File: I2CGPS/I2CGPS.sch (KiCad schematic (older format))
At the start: 1 part, among them P1 CONN_01X05

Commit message: I2C-GPS initial design
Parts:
- added C1, C2: C, Capacitors_SMD:C_1210_HandSoldering, symbol C
- added P2, P3: CONN_01X09, Pin_Headers:Pin_Header_Straight_1x09, symbol CONN_01X09
- added U1: GY-NEO6MV2, ADEM:GY-NEO6MV2, symbol GY-NEO6MV2
- added uP1: ARDUPROMINI-6, ArduProMiniTKB:ArduProMini-6, symbol ARDUPROMINI-6
- P1: footprint (none) -> Pin_Headers:Pin_Header_Straight_1x05
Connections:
- net VCC: now reaches P1.1 (P1)
- net VCC: now also C1.1, C2.1, P3.1 (P1), U1.1 (VCC), uP1.22 (Vcc2)
- net SDA: now reaches P1.2 (P2)
- net SDA: now also P2.8 (P8), uP1.11 (D2)
- net SCL: now reaches P1.3 (P3)
- net SCL: now also P2.7 (P7), uP1.12 (D3)
- net INT: now reaches P1.4 (P4)
- net INT: now also P2.6 (P6), uP1.13 (D4)
- net GND: now reaches P1.5 (P5)
- net GND: now also C1.2, C2.2, P2.9 (P9), U1.4 (GND), uP1.10 (GND), uP1.20 (GND3)
- new net: P2.5 (P5), uP1.14 (D5)
- new net: P2.4 (P4), uP1.15 (D6)
- new net: P2.3 (P3), uP1.16 (D7)
- new net: P2.2 (P2), uP1.17 (D8)
- new net: P2.1 (P1), uP1.18 (D9)
- new net: P3.2 (P2), uP1.23 (A3)
- new net: P3.3 (P3), uP1.24 (A2)
- new net: P3.4 (P4), uP1.25 (A1)
- new net: P3.5 (P5), uP1.26 (A0)
- new net: P3.6 (P6), uP1.27 (D13)
- new net: P3.7 (P7), uP1.28 (D12)
- new net: P3.8 (P8), uP1.29 (D11)
- new net: P3.9 (P9), uP1.30 (D10)
- new net RX: U1.2 (RX), uP1.8 (RX1)
- new net TX: U1.3 (TX), uP1.7 (TX0)

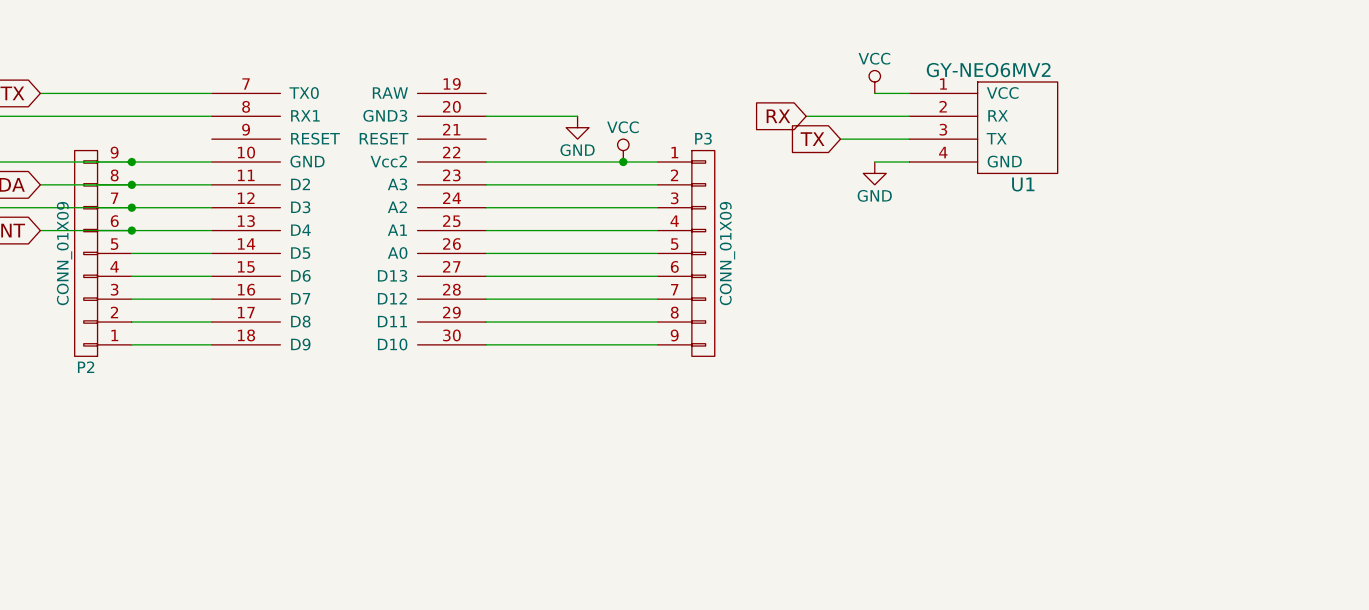
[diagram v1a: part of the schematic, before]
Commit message: IC2 GPS with power down fet
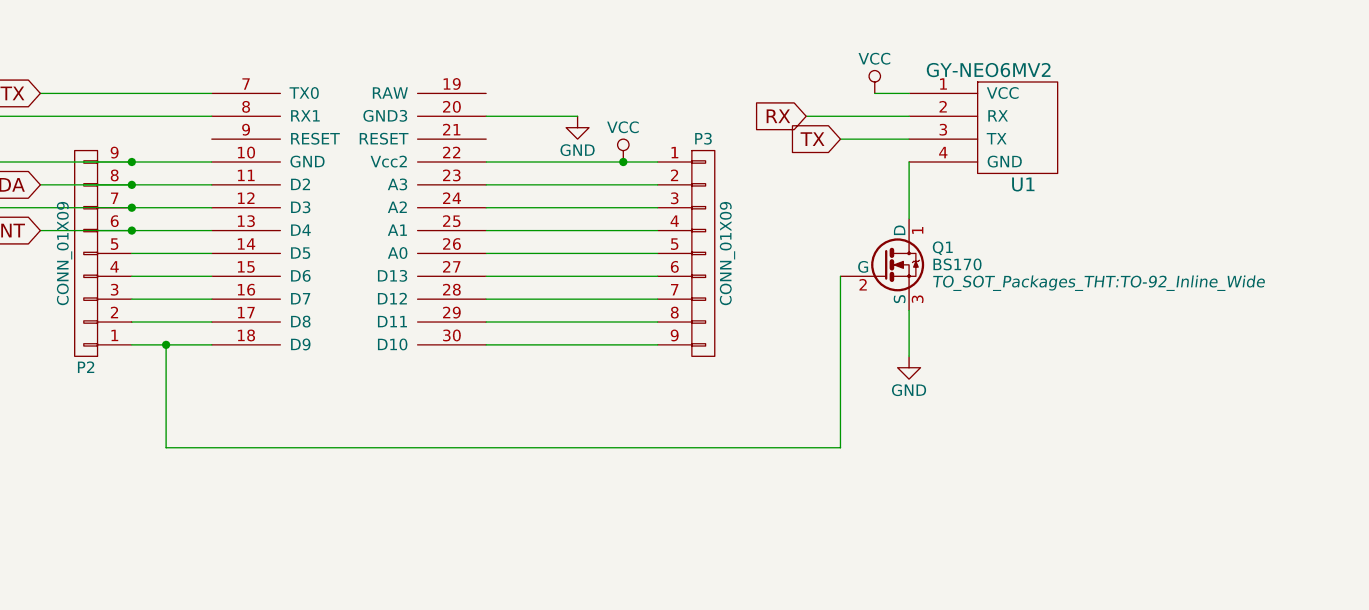
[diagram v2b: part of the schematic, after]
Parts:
- added Q1: BS170, TO_SOT_Packages_THT:TO-92_Inline_Wide, symbol BS170
- P1: footprint Pin_Headers:Pin_Header_Straight_1x05 -> Pin_Headers:Pin_Header_Angled_1x05
- uP1: footprint ArduProMiniTKB:ArduProMini-6 -> ArduProMiniTKB:ArduProMini
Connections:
- net GND: now also Q1.3 (S); no longer U1.4 (GND)
- net at P2.1 (P1), uP1.18 (D9): now also Q1.2 (G)
- new net: Q1.1 (D), U1.4 (GND)
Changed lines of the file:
@@
 F 0 "P1" H 1800 1900 50  0000 C CNN
 F 1 "CONN_01X05" V 1900 1600 50  0000 C CNN
-F 2 "Pin_Headers:Pin_Header_Straight_1x05" H 1800 1600 50  0001 C CNN
+F 2 "Pin_Headers:Pin_Header_Angled_1x05" H 1800 1600 50  0001 C CNN
 F 3 "" H 1800 1600 50  0000 C CNN
 	1    1800 1600
@@
 F 0 "uP1" H 3200 2500 60  0000 C CNN
 F 1 "ARDUPROMINI-6" H 3400 2600 60  0000 C CNN
-F 2 "ArduProMiniTKB:ArduProMini-6" H 3400 2600 60  0001 C CNN
+F 2 "ArduProMiniTKB:ArduProMini" H 3400 2600 60  0001 C CNN
 F 3 "" H 3400 2600 60  0000 C CNN
 	1    3400 2600
@@
 L GND #PWR03
 U 1 1 57BB5D8A
-P 5100 4000
-F 0 "#PWR03" H 5100 3750 50  0001 C CNN
-F 1 "GND" H 5100 3850 50  0000 C CNN
-F 2 "" H 5100 4000 50  0000 C CNN
-F 3 "" H 5100 4000 50  0000 C CNN
-	1    5100 4000
+P 5250 4850
+F 0 "#PWR03" H 5250 4600 50  0001 C CNN
+F 1 "GND" H 5250 4700 50  0000 C CNN
+F 2 "" H 5250 4850 50  0000 C CNN
+F 3 "" H 5250 4850 50  0000 C CNN
+	1    5250 4850
 	1    0    0    -1
 $EndComp
@@
 Wire Wire Line
 	5100 3700 5250 3700
-Wire Wire Line
-	5100 4000 5250 4000
 Wire Wire Line
 	3400 3800 3800 3800
@@
 	1850 4700 2200 4700
 Wire Wire Line
-	2200 4800 1850 4800
-Wire Wire Line
 	3400 4800 4150 4800
 Wire Wire Line
@@
 	4150 4100 3400 4100
 Connection ~ 4000 4000
+$Comp
+L BS170 Q1
+U 1 1 57BC9FCB
+P 5150 4450
+F 0 "Q1" H 5350 4525 50  0000 L CNN
+F 1 "BS170" H 5350 4450 50  0000 L CNN
+F 2 "TO_SOT_Packages_THT:TO-92_Inline_Wide" H 5350 4375 50  0000 L CIN
+F 3 "" H 5150 4450 50  0000 L CNN
+	1    5150 4450
+	1    0    0    -1
+$EndComp
+Wire Wire Line
+	5250 4000 5250 4250
+Wire Wire Line
+	5250 4650 5250 4850
+Wire Wire Line
+	4950 5250 4950 4500
+Wire Wire Line
+	2000 5250 4950 5250
+Wire Wire Line
+	2200 4800 1850 4800
+Wire Wire Line
+	2000 4800 2000 5250
+Connection ~ 2000 4800
 $EndSCHEMATC

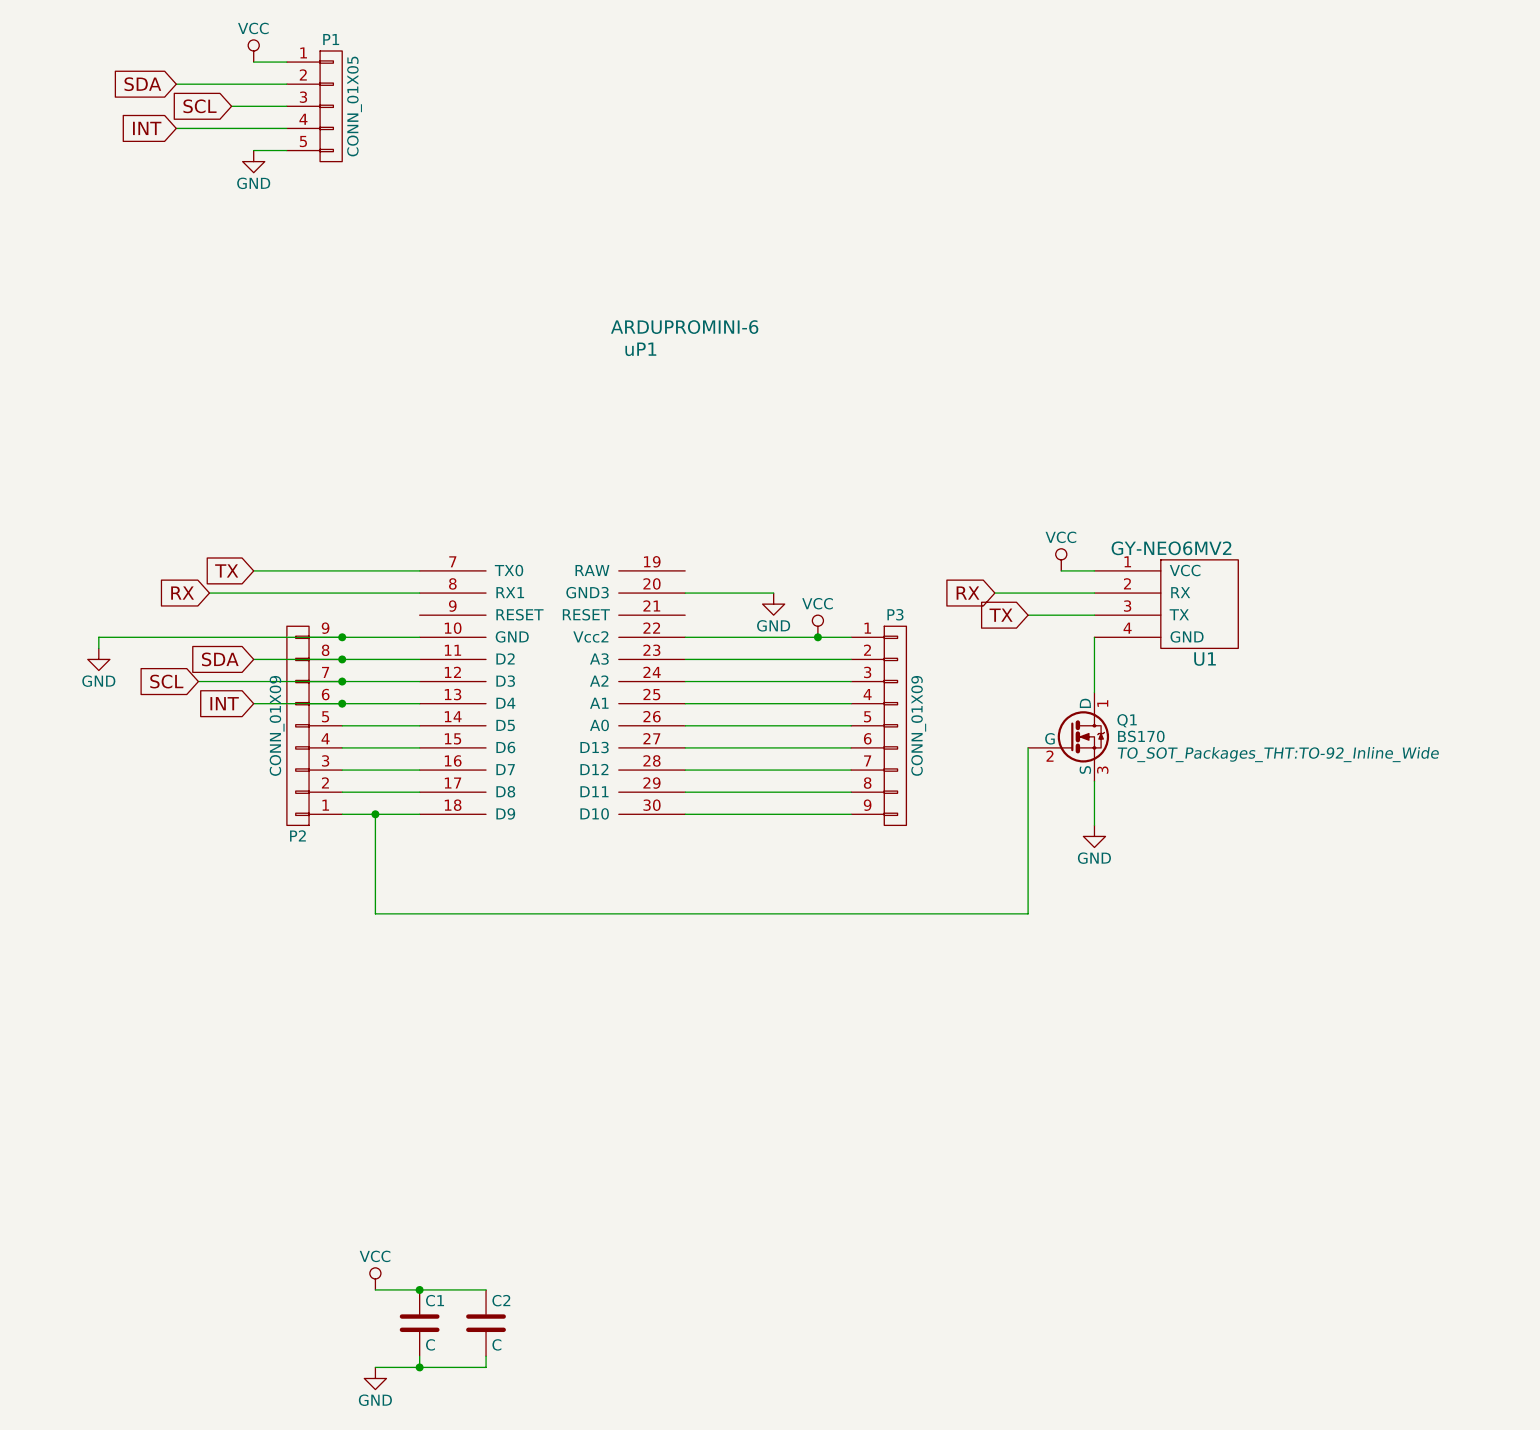
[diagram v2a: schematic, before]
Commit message: resized to particle sensor and panelized
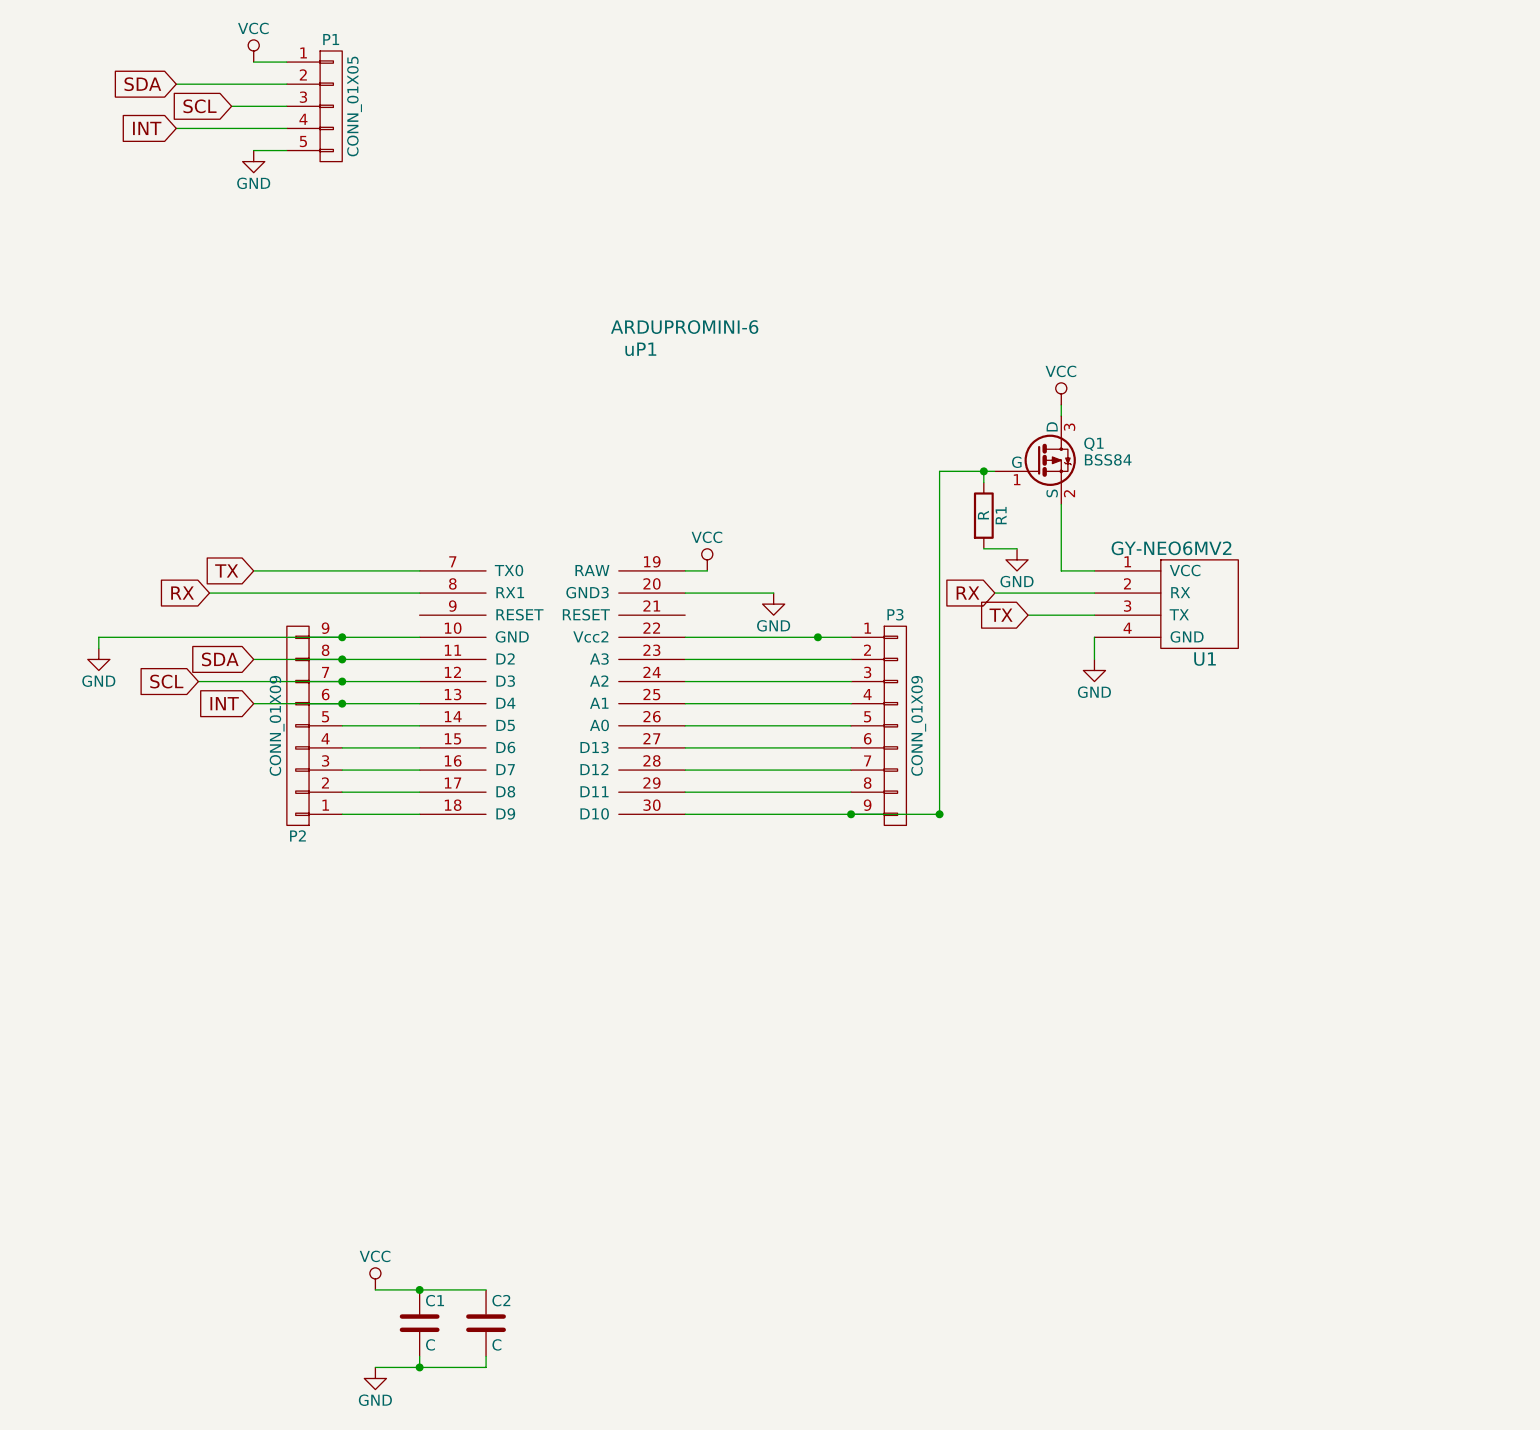
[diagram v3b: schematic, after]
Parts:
- removed Q1: BS170, TO_SOT_Packages_THT:TO-92_Inline_Wide, symbol BS170
- added Q1: BSS84, TO_SOT_Packages_SMD:SOT-23, symbol BSS84
- added R1: R, Resistors_SMD:R_1210_HandSoldering, symbol R
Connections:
- net GND: now also U1.4 (GND), R1.2
- net VCC: now also uP1.19 (RAW), Q1.3 (D); no longer P3.1 (P1), U1.1 (VCC), uP1.22 (Vcc2)
- net at P3.9 (P9), uP1.30 (D10): now also Q1.1 (G), R1.1
- new net: P3.1 (P1), uP1.22 (Vcc2)
- new net: Q1.2 (S), U1.1 (VCC)
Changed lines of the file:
@@
 L GND #PWR03
 U 1 1 57BB5D8A
-P 5250 4850
-F 0 "#PWR03" H 5250 4600 50  0001 C CNN
-F 1 "GND" H 5250 4700 50  0000 C CNN
-F 2 "" H 5250 4850 50  0000 C CNN
-F 3 "" H 5250 4850 50  0000 C CNN
-	1    5250 4850
+P 5250 4100
+F 0 "#PWR03" H 5250 3850 50  0001 C CNN
+F 1 "GND" H 5250 3950 50  0000 C CNN
+F 2 "" H 5250 4100 50  0000 C CNN
+F 3 "" H 5250 4100 50  0000 C CNN
+	1    5250 4100
 	1    0    0    -1
 $EndComp
@@
 L VCC #PWR07
 U 1 1 57BB5EEB
-P 5100 3700
-F 0 "#PWR07" H 5100 3550 50  0001 C CNN
-F 1 "VCC" H 5100 3850 50  0000 C CNN
-F 2 "" H 5100 3700 50  0000 C CNN
-F 3 "" H 5100 3700 50  0000 C CNN
-	1    5100 3700
+P 5100 2950
+F 0 "#PWR07" H 5100 2800 50  0001 C CNN
+F 1 "VCC" H 5100 3100 50  0000 C CNN
+F 2 "" H 5100 2950 50  0000 C CNN
+F 3 "" H 5100 2950 50  0000 C CNN
+	1    5100 2950
 	1    0    0    -1
 $EndComp
@@
 L VCC #PWR08
 U 1 1 57BB5F11
-P 4000 4000
-F 0 "#PWR08" H 4000 3850 50  0001 C CNN
-F 1 "VCC" H 4000 4150 50  0000 C CNN
-F 2 "" H 4000 4000 50  0000 C CNN
-F 3 "" H 4000 4000 50  0000 C CNN
-	1    4000 4000
+P 3500 3700
+F 0 "#PWR08" H 3500 3550 50  0001 C CNN
+F 1 "VCC" H 3500 3850 50  0000 C CNN
+F 2 "" H 3500 3700 50  0000 C CNN
+F 3 "" H 3500 3700 50  0000 C CNN
+	1    3500 3700
 	1    0    0    -1
 $EndComp
@@
 Wire Wire Line
 	1450 4300 2200 4300
-Wire Wire Line
-	5100 3700 5250 3700
 Wire Wire Line
 	3400 3800 3800 3800
@@
 	1850 4700 2200 4700
 Wire Wire Line
-	3400 4800 4150 4800
+	3400 4800 4550 4800
 Wire Wire Line
 	4150 4700 3400 4700
@@
 	4150 4100 3400 4100
 Connection ~ 4000 4000
-$Comp
-L BS170 Q1
-U 1 1 57BC9FCB
-P 5150 4450
-F 0 "Q1" H 5350 4525 50  0000 L CNN
-F 1 "BS170" H 5350 4450 50  0000 L CNN
-F 2 "TO_SOT_Packages_THT:TO-92_Inline_Wide" H 5350 4375 50  0000 L CIN
-F 3 "" H 5150 4450 50  0000 L CNN
-	1    5150 4450
-	1    0    0    -1
-$EndComp
-Wire Wire Line
-	5250 4000 5250 4250
-Wire Wire Line
-	5250 4650 5250 4850
-Wire Wire Line
-	4950 5250 4950 4500
-Wire Wire Line
-	2000 5250 4950 5250
 Wire Wire Line
 	2200 4800 1850 4800
-Wire Wire Line
-	2000 4800 2000 5250
-Connection ~ 2000 4800
+$Comp
+L BSS84 Q1
+U 1 1 57C1A8ED
+P 5000 3200
+F 0 "Q1" H 5200 3275 50  0000 L CNN
+F 1 "BSS84" H 5200 3200 50  0000 L CNN
+F 2 "TO_SOT_Packages_SMD:SOT-23" H 5200 3125 50  0001 L CIN
+F 3 "" H 5000 3200 50  0000 L CNN
+	1    5000 3200
+	1    0    0    -1
+$EndComp
+Wire Wire Line
+	5100 2950 5100 3000
+Wire Wire Line
+	5100 3400 5100 3700
+Wire Wire Line
+	5100 3700 5250 3700
+Wire Wire Line
+	5250 4000 5250 4100
+Wire Wire Line
+	4550 3250 4800 3250
+$Comp
+L R R1
+U 1 1 57C1AE43
+P 4750 3450
+F 0 "R1" V 4830 3450 50  0000 C CNN
+F 1 "R" V 4750 3450 50  0000 C CNN
+F 2 "Resistors_SMD:R_1210_HandSoldering" V 4680 3450 50  0001 C CNN
+F 3 "" H 4750 3450 50  0000 C CNN
+	1    4750 3450
+	1    0    0    -1
+$EndComp
+Wire Wire Line
+	4750 3300 4750 3250
+Connection ~ 4750 3250
+$Comp
+L GND #PWR010
+U 1 1 57C1AF1D
+P 4900 3600
+F 0 "#PWR010" H 4900 3350 50  0001 C CNN
+F 1 "GND" H 4900 3450 50  0000 C CNN
+F 2 "" H 4900 3600 50  0000 C CNN
+F 3 "" H 4900 3600 50  0000 C CNN
+	1    4900 3600
+	1    0    0    -1
+$EndComp
+Wire Wire Line
+	4900 3600 4750 3600
+Connection ~ 4550 4800
+Wire Wire Line
+	4550 4800 4550 3250
+Connection ~ 4150 4800
+Wire Wire Line
+	3500 3700 3400 3700
 $EndSCHEMATC
